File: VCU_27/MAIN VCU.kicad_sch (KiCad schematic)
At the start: 64 parts, among them J1 Micro_SD_Card_Det_Hirose_DM3AT, J3 JTAG_CONN, P1 USB_C_Plug_USB2.0, Q1 NMOS, Q2 NMOS, Q3 NMOS, Q4 NMOS, SW1 SW_SPDT_321, SW2 SW_Push, U1 STM32H723VGTx, U2 ESP32-S3-MINI-1U

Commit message: VCU Digital input and usb esd protection
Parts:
- removed C14: 10uF, symbol Device:C
- removed C15, C16: 1uf, symbol Device:C
- removed D2, D3: D_Schottky, symbol Device:D_Schottky
- removed Q2, Q3, Q4: NMOS, symbol Simulation_SPICE:NMOS
- removed R24: 10k, symbol Device:R
- removed R25: 100, symbol Device:R
- removed RESET1, boot1: SW_Push, symbol Switch:SW_Push
- removed U2: ESP32-S3-MINI-1U, RF_Module:ESP32-S2-MINI-1U, symbol RF_Module:ESP32-S3-MINI-1U
- added C22, C23: 20pF, symbol Device:C
- added C24: 1uf, symbol Device:C
- added D10, D11, D2, D9: SMF15A, Diode_SMD:D_SMF, symbol Diode:SMF15A
- added D3: SMF5V0A, Diode_SMD:D_SMF, symbol Diode:SMF5V0A
- added D5, D6, D7, D8: D_Schottky, symbol Device:D_Schottky
- added J2: 1746979-1, 17469791, symbol 1746979-1:1746979-1
- added Q5: BTS3035TFATMA1, BTS3035TFATMA1, symbol BTS3035TFATMA1:BTS3035TFATMA1
- added Q6: BSP75N, Package_TO_SOT_SMD:SOT-223, symbol Transistor_FET_Other:BSP75N
- added R26: 10k, symbol Device:R
- added SW3: SW_Push, symbol Switch:SW_Push
- added U3: USBLC6-2SC6, Package_TO_SOT_SMD:SOT-23-6, symbol Power_Protection:USBLC6-2SC6
- added U4: XIAO-ESP32-S3-SMD, Seeed_Studio_XIAO_Series:XIAO-ESP32-S3-SMD, symbol Seeed_Studio_XIAO_Series:XIAO-ESP32-S3-SMD
- added Y1: 25MHz, symbol Device:Crystal_GND24
- C13: value 0.1uF -> 100nF
- C17: value 10nF -> 100nF
- R17: value 1k -> 2K
- R18, R2: value 10k -> 1K
- R19: value 100 -> 1K
- R20: value 1k -> 10k
- R21: value 10k -> 68K
- R22: value 100 -> 47K
- R23: value 1k -> 5.1K
- R4: value 1k5 -> 2K
- R8: value 1K -> 220K
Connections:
- net +3.3V: now also R17.1, R18.1, R19.2, R20.1; no longer C13.1, D4.2 (A), R2.1
- net +5V: now also D4.2 (A), R23.1, J2.41, J2.51, U3.5 (VBUS)
- net Analog Sensor -: no longer D4.1 (K)
- net Digin_3: now also D2.1 (A1), D8.1 (K); no longer U1.96 (PB9)
- net Digin_5: now also D11.1 (A1), D5.1 (K), J2.6; no longer U1.93 (PB7)
- net Digin_6: now also D7.1 (K), D9.1 (A1), J2.25; no longer U1.92 (PB6)
- net Digin_7: now also D10.1 (A1), D6.1 (K), J2.7; no longer U1.91 (PB5)
- net ESP32_RX: now also U4.8 (D7)
- net ESP32_TX: now also U4.7 (D6)
- net GND: now also C22.2, C23.2, C24.2, D10.2 (A2), D11.2 (A2), D2.2 (A2), D3.2 (A2), D9.2 (A2), J2.48, J2.60, Q5.3 (GND), R26.2, SW3.1, U3.2 (GND), U4.13 (GND), U4.18 (GND), U4.24 (GND), U4.25 (PAD); no longer R18.2
- net PWM: no longer R17.1, R20.1, R23.1
- net TIM15_CH1: now also Q5.1 (IN), R26.1
- net at U1.12 (PH0): now also C23.1, Y1.1
- net at U1.13 (PH1): now also C22.1, Y1.3
- net at R2.2: now also R21.1, R22.2
- net Selector pin: now reaches R23.2
- net Selector pin: now also R22.1, D3.1 (A1)
- removed net USB_D+: P1.A6 (D+), R4.2, U1.71 (PA12)
- net USB_D-: no longer names the net of P1.A7 (D-)
- net USB_D-: now also U3.1 (I/O1); no longer U1.70 (PA11)
- new net: P1.A6 (D+), U3.3 (I/O2)
- new net: U1.71 (PA12), U3.4 (I/O2)
- new net: U1.70 (PA11), U3.6 (I/O1)
- new net: D6.2 (A), R17.2, U1.91 (PB5)
- new net: D7.2 (A), R18.2, U1.92 (PB6)
- new net: D5.2 (A), R4.2, U1.93 (PB7)
- new net: Y1.2 (G), Y1.4 (G)
- new net: D4.1 (K), U4.14 (VBUS)
- new net: SW3.2, U4.17 (EN)
- new net: Q6.3 (SOURCE), Q6.4 (SOURCE)
- new net: C24.1, R20.2
- new net ADC_INPUT: C13.1, R2.1
- new net Digin Pin 14: D8.2 (A), R19.1, U1.96 (PB9)
- new net Water_Pump_PWM: Q5.2 (OUT)
- no-connect marks 54 -> 17
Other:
- note added: "Rad Temp IN"
- moved on the sheet: C17, J3, P1, R3, R5, R8

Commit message: digital inputs and Low side drivers and High side drivers and ADC
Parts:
- removed Q6: BSP75N, Package_TO_SOT_SMD:SOT-223, symbol Transistor_FET_Other:BSP75N
- added C14, C15: 100nf, symbol Device:C
- added C16, C25, C26, C28, C29, C31: 10nF, symbol Device:C
- added C27, C30, C32: 1uF, symbol Device:C
- added D12, D15, D17, D18, D20, D22: SMF15A, Diode_SMD:D_SMF, symbol Diode:SMF15A
- added D13, D14, D16, D19, D21, D23, D26: D_Schottky, symbol Device:D_Schottky
- added D24: SMF5V0A, Diode_SMD:D_SMF, symbol Diode:SMF5V0A
- added D25: SM15T7V5A, Diode_SMD:ST_D_SMC, symbol Diode:SM15T7V5A
- added IC1, IC2, IC3: BV1HAL45EFJ-E2, SOIC127P600X100-9N, symbol BV1HAL45EFJ-E2:BV1HAL45EFJ-E2
- added Q6, Q7, Q8: BTS3035TFATMA1, BTS3035TFATMA1, symbol BTS3035TFATMA1:BTS3035TFATMA1
- added R24: 2k, symbol Device:R
- added R25: 1k, symbol Device:R
- added R27, R30, R32: 6.8K, symbol Device:R
- added R28, R33: 15K, symbol Device:R
- added R29, R31, R36, R44, R49, R53: 15k, symbol Device:R
- added R34: 10K, symbol Device:R
- added R35, R40, R41, R42, R45, R46, R47, R50, R51, R54: 10k, symbol Device:R
- added R37: 5.1K, symbol Device:R
- added R38: 20K, symbol Device:R
- added R39: 30K, symbol Device:R
- added R43, R48, R52: 200k, symbol Device:R
- R18: value 1K -> 2K
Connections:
- net Digin_4 is gone; now on net Digin_8: U1.95 (PB8)
- net +3.3V: now also R24.1, R25.1, R37.2, R46.1, R50.1, R54.1
- net ADC_IN: now also C14.1, C15.1, D26.1 (K), R35.2, R36.1, R38.2, R39.1
- net Digin_10: now also D19.1 (K)
- net Digin_12: now also D21.1 (K)
- net Digin_3: now also J2.27
- net Digin_8: now also D13.2 (A), D14.2 (A), R24.2, R25.2
- net GND: now also J2.120, J2.121, J2.2, J2.4, J2.5, J2.70, J2.74, J2.75, C14.2, C15.2, C16.2, C25.2, C26.2, C27.2, C28.2, C29.2, C30.2, C31.2, C32.2, D12.2 (A2), D15.2 (A2), D17.2 (A2), D18.2 (A2), D20.2 (A2), D22.2 (A2), D24.2 (A2), D25.2 (A2), D26.2 (A), IC1.3 (GND_1), IC2.3 (GND_1), IC3.3 (GND_1), Q6.3 (GND), Q7.3 (GND), Q8.3 (GND), R27.1, R30.1, R32.1, R34.1, R36.2, R39.2, R40.1, R41.1, R42.1, R43.2, R44.1, R45.2, R47.2, R48.2, R49.1, R51.2, R52.2, R53.1
- net at J2.10: now also D20.1 (A1), R31.1
- net at J2.26: now also D14.1 (K), D15.1 (A1)
- net at J2.46: now also D18.1 (A1), R29.1
- net at J2.65: now also D17.1 (A1), R28.1
- net at J2.67: now also J2.68, D22.1 (A1), R33.1
- net at J2.8: now also D12.1 (A1), D13.1 (K)
- new net: IC1.1 (SS), R44.2
- new net: IC1.2 (ILIM), R43.1
- new net: D21.2 (A), R31.2, R32.2
- new net: D16.2 (A), R27.2, R28.2
- new net: D23.2 (A), R33.2, R34.2
- new net: IC3.1 (SS), R53.2
- new net: D19.2 (A), R29.2, R30.2
- new net: IC3.2 (ILIM), R52.1
- new net: IC2.2 (ILIM), R48.1
- new net: IC2.1 (SS), R49.2
- new net +12V: C27.1, C30.1, C32.1, IC1.9 (VIN), IC2.9 (VIN), IC3.9 (VIN)
- new net BSE1: D24.1 (A1), R35.1
- new net BSE2: D25.1 (A1), R37.1, R38.1
- new net Connector: C28.1, C29.1, C31.1, IC1.7 (OUT_1), IC1.8 (OUT_2), IC2.7 (OUT_1), IC2.8 (OUT_2), IC3.7 (OUT_1), IC3.8 (OUT_2)
- new net Connector_pin: C16.1, C25.1, C26.1, Q6.2 (OUT), Q7.2 (OUT), Q8.2 (OUT)
- new net Digin_9: D16.1 (K), D23.1 (K)
- new net STM32_GPIO_IN: IC1.4 (FLAG), IC2.4 (FLAG), IC3.4 (FLAG), R46.2, R50.2, R54.2
- new net STM32_GPIO_OUT: IC1.5 (EN), IC2.5 (EN), IC3.5 (EN), R45.1, R47.1, R51.1
- new net STM32_digin: Q6.1 (IN), Q7.1 (IN), Q8.1 (IN), R40.2, R41.2, R42.2
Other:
- note added: "ACC1"
- note added: "ACC2 & Brake"
- note added: "DTI"
- note added: "Frequency inputs"
- note added: "LAMP CHECK"
- note added: "Low Side Drivers"
- note added: "REGEN INDICATOR"
- note added: "Sensor Ground"
- note added: "Water Pump PWM"
- moved on the sheet: C1, C10, C11, C12, C13, C17, C18, C19, C2, C20, C21, C22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

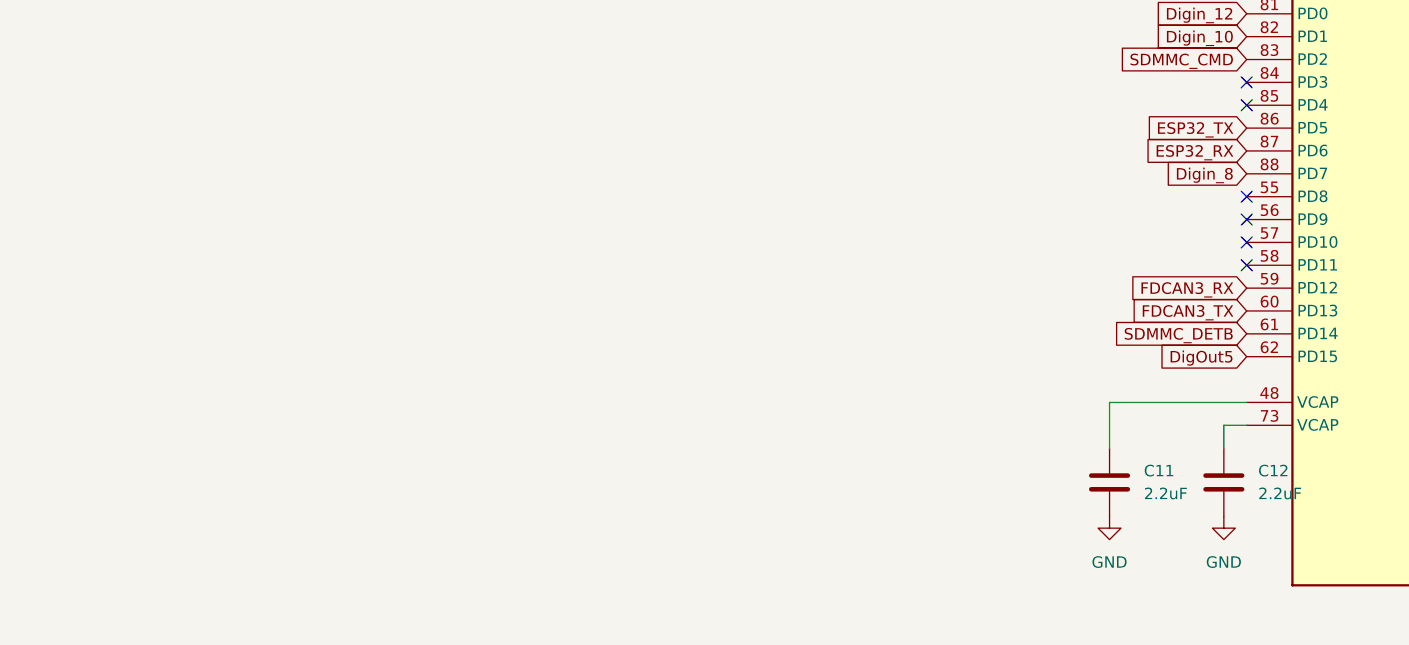
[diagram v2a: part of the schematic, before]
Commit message: added CAN Transciever
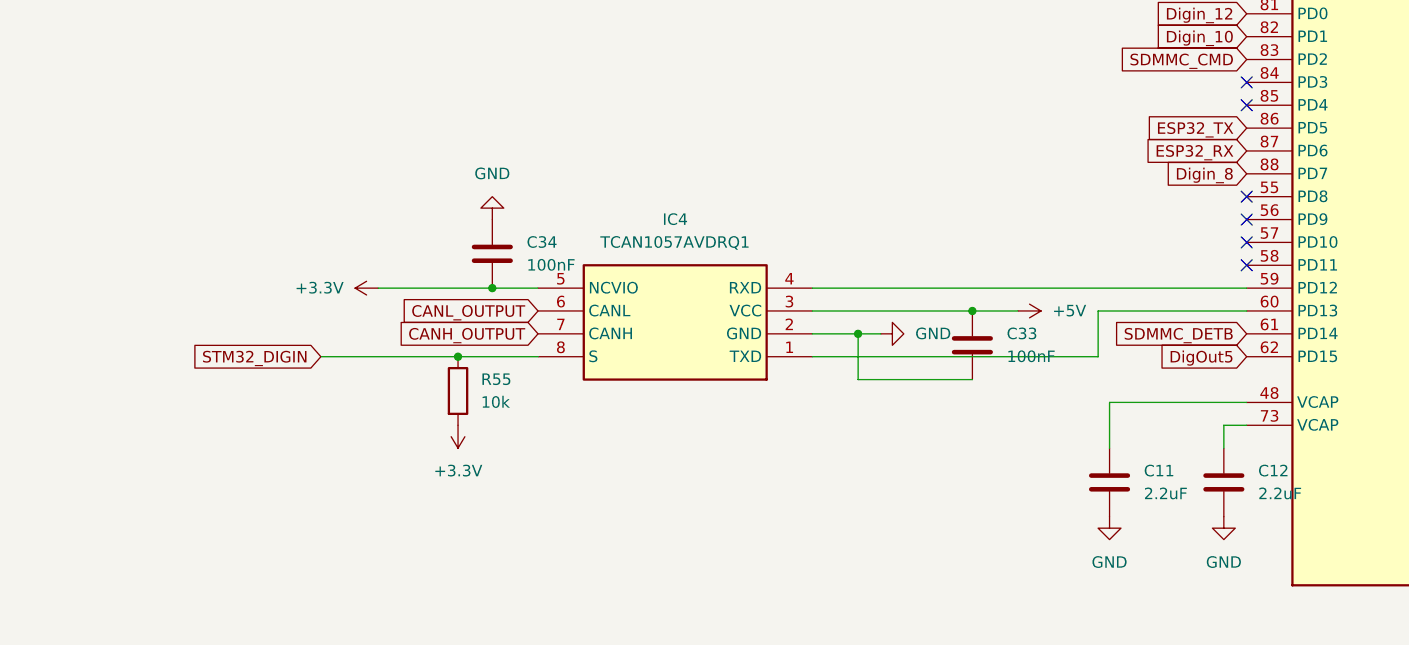
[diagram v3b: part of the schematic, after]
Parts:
- added C33, C34: 100nF, symbol Device:C
- added IC4: TCAN1057AVDRQ1, SOIC127P600X175-8N, symbol TCAN1057AVDRQ1:TCAN1057AVDRQ1
- added R55: 10k, symbol Device:R
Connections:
- net +3.3V: now also C34.2, IC4.5 (NCVIO), R55.2
- net +5V: now also C33.1, IC4.3 (VCC)
- net GND: now also C33.2, C34.1, IC4.2 (GND)
- net FDCAN3_RX: no longer names the net of U1.59 (PD12)
- net FDCAN3_RX: now also IC4.4 (RXD)
- net FDCAN3_TX: no longer names the net of U1.60 (PD13)
- net FDCAN3_TX: now also IC4.1 (TXD)
- new net CANH_OUTPUT: IC4.7 (CANH)
- new net CANL_OUTPUT: IC4.6 (CANL)
- new net STM32_DIGIN: IC4.8 (S), R55.1

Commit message: Frequency Inputs
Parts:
- added C35, C36, C37, C38: 1nF, symbol Device:C
- added D27, D34, D38, D42, D46: SMF15A, Diode_SMD:D_SMF, symbol Diode:SMF15A
- added D28, D29, D30, D31, D32, D33, D35, D36, D37, D39, D40, D41, D43, D44, D45: D_Schottky, symbol Device:D_Schottky
- added R56, R59, R62, R65, R68: 10k, symbol Device:R
- added R57, R58, R61, R64, R67: 15k, symbol Device:R
- added R60, R63, R66, R69: 2.2k, symbol Device:R
- R9: value 100 -> 2.2k
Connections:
- net DAC_OUT is gone; now on net Connector: R9.2
- net +3.3V: now also D30.1 (K), D31.1 (K), D35.1 (K), D39.1 (K), D43.1 (K)
- net +5V: now also D28.2 (A), D33.2 (A), D37.2 (A), D41.2 (A), D45.2 (A)
- net Connector: now also D27.1 (A1), D34.1 (A1), D38.1 (A1), D42.1 (A1), D46.1 (A1), R56.2, R59.2, R60.2, R62.2, R63.2, R65.2, R66.2, R68.2, R69.2
- net GND: now also C35.2, C36.2, C37.2, C38.2, D27.2 (A2), D29.2 (A), D32.2 (A), D34.2 (A2), D36.2 (A), D38.2 (A2), D40.2 (A), D42.2 (A2), D44.2 (A), D46.2 (A2), R57.2, R58.2, R61.2, R64.2, R67.2
- net Analog_Output: no longer names the net of R9.1
- net Analog_Output: now also D28.1 (K); no longer C18.1
- new net: D41.1 (K), R66.1
- new net: D37.1 (K), R63.1
- new net: D33.1 (K), R60.1
- new net: D45.1 (K), R69.1
- new net STM32_TIM: C18.1, C35.1, C36.1, C37.1, C38.1, D29.1 (K), D30.2 (A), D31.2 (A), D32.1 (K), D35.2 (A), D36.1 (K), D39.2 (A), D40.1 (K), D43.2 (A), D44.1 (K), R56.1, R57.1, R58.1, R59.1, R61.1, R62.1, R64.1, R65.1, R67.1, R68.1
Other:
- note added: "BSE1"
- note added: "BSE2"
- note added: "HIGH SIDE DRIVERS"
- note removed: "DAC Output Filtering"
- moved on the sheet: C13, C14, C15, C17, C20, C21, D1, D24, D25, D26, D3, Q1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

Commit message: stm32 net label
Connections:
- net Digin_10: no longer U1.82 (PD1)
- net Digin_12: no longer U1.81 (PD0)
- net Digin_8: no longer U1.88 (PD7), U1.95 (PB8)
- net SDMMC_CLK: no longer U1.80 (PC12)
- net SDMMC_D2: no longer U1.78 (PC10)
- net SDMMC_D3: no longer U1.79 (PC11)
- net TIM15_CH1: no longer Q5.1 (IN), R26.1
- net SD_CD: now reaches U1.57 (PD10)
- net SD_WP: now reaches U1.58 (PD11)
- net USART2_CTS: now reaches U1.84 (PD3)
- net USART2_RTS: now reaches U1.85 (PD4)
- net ADC2_IN19 renamed BACK_BRAKE_PRESSURE
- net ADC2_INP14 renamed OUTLET_TEMPERATURE
- net ADC2_INP15 renamed FRONT_BRAKE_PRESSURE
- net ADC2_INP7 renamed SUSPENSION_BR
- net ADC2_INP8 renamed STEERING_ANGLE
- net ADC3_INP11 renamed INLET_TEMPERATURE
- net ADC_INP17 renamed ADC1_INP17
- net ADC_INP3 renamed SUSPENSION_FL
- net ADC_INP4 renamed SUSPENSION_FR
- net CAN2_RX renamed FDCAN2_RX
- net CAN2_TX renamed FDCAN2_TX
- net DigOut_4 renamed DIGOUT4
- net Digin_1 renamed DIGIN1
- net Digin_2 renamed DIGIN2
- net Digout_1 renamed DIGOUT1
- net Digout_2 renamed DIGOUT2
- net Digout_3 renamed DIGOUT3
- net OCTOSPI_IO4 renamed OCTOSPIM_PI_1O4
- net OCTOSPI_IO5 renamed OCTOSPIM_P1_1O5
- net PWM2_CH1 renamed TIM12_CH1
- net PWM2_CH2 renamed TIM12_CH2
- net PWM2_CH3: no longer names the net of U1.40 (PE10)
- net PWM2_CH3: no longer U1.46 (PB10)
- net PWM3_CH2 renamed TIM3_CH2
- net PWM_CH1 renamed Pump_PWM
- net Pump_PWM: now also Q5.1 (IN), R26.1; no longer U1.39 (PE9)
- net PWM_CH2 renamed TIM1_CH2
- net PWM_CH3 renamed TIM1_CH3
- net PWM_CH4 renamed TIM1_CH4
- net TIM1_CH4: no longer U1.47 (PB11)
- net SDMMC_D0 renamed SDMMC1_D0
- net SDMMC_D1 renamed SDMMC1_D1
- new net DIGIN10: U1.82 (PD1)
- new net DIGIN12: U1.81 (PD0)
- new net DIGIN8: U1.88 (PD7)
- new net Digin_4: U1.95 (PB8)
- new net SDMMC1_CLK: U1.80 (PC12)
- new net SDMMC1_D2: U1.78 (PC10)
- new net SDMMC1_D3: U1.79 (PC11)
- new net TIM1_CH1: U1.39 (PE9)
- new net TIM2_CH3: U1.46 (PB10)
- new net TIM2_CH4: U1.47 (PB11)
- no-connect marks 17 -> 14
